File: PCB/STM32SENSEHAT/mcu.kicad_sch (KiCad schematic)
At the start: 5 parts, among them J2 Conn_01x33_Female, J3 Conn_01x33_Female, J4 Conn_01x33_Female, J5 Conn_01x33_Female, J6 Conn_01x10_Pin

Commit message: rework of top level sheet, MCU, power and sensor sheet
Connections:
- net PA10 renamed STM_UART_TX
- net PA9 renamed STM_UART_RX
- net PF6 renamed STM_I2C_SDA
- net PF7 renamed STM_I2C_SCL
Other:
- note added: "I/O INTERFACE"
- note added: "MCU"
- note removed: "16 units apart = 2.54 x 16"
- note removed: "Disco_Connection"
- company: (none) -> IMPERIUM
- title: (none) -> MCU MODULE
- moved on the sheet: J2, J3, J4, J5, J6

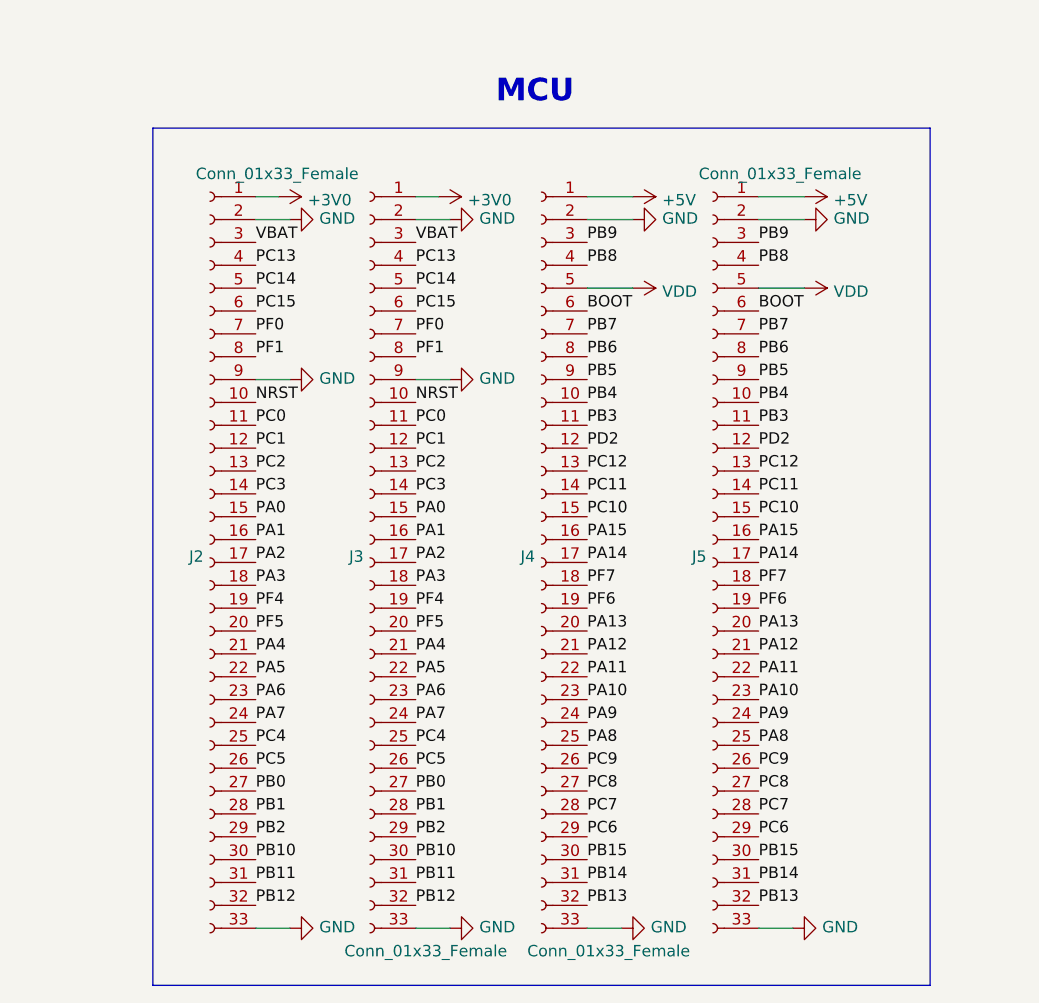
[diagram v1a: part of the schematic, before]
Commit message: Modified the connector symbol for STM32 from 66 pins to 48 pins
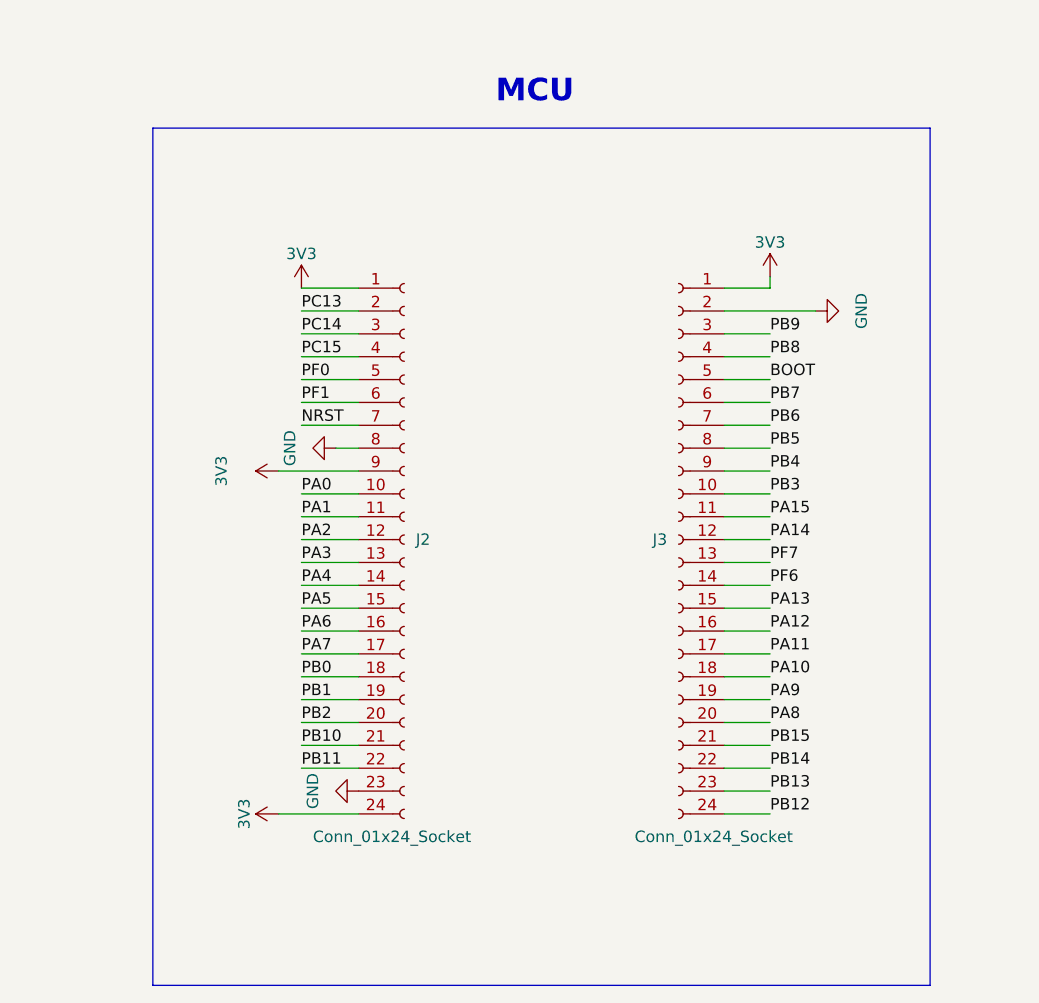
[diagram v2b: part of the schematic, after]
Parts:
- removed J2, J5: Conn_01x33_Female, Connector_PinHeader_2.54mm:PinHeader_1x33_P2.54mm_Vertical, symbol Connector:Conn_01x33_Female
- removed J3, J4: Conn_01x33_Female, Connector_PinSocket_2.54mm:PinSocket_1x33_P2.54mm_Vertical, symbol Connector:Conn_01x33_Female
- added J2, J3: Conn_01x24_Socket, symbol Connector:Conn_01x24_Socket
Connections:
- net BOOT: now also J3.5 (Pin_5)
- net GND: now also J2.23 (Pin_23), J2.8 (Pin_8), J3.2 (Pin_2)
- net NRST: now also J2.7 (Pin_7)
- net PA0: now also J2.10 (Pin_10)
- net PA1: now also J2.11 (Pin_11)
- net PA11: now also J3.17 (Pin_17)
- net PA12: now also J3.16 (Pin_16)
- net PA13: now also J3.15 (Pin_15)
- net PA14: now also J3.12 (Pin_12)
- net PA15: now also J3.11 (Pin_11)
- net PA2: now also J2.12 (Pin_12)
- net PA3: now also J2.13 (Pin_13)
- net PA4: now also J2.14 (Pin_14)
- net PA5: now also J2.15 (Pin_15)
- net PA6: now also J2.16 (Pin_16)
- net PA7: now also J2.17 (Pin_17)
- net PA8: now also J3.20 (Pin_20)
- net PB0: now also J2.18 (Pin_18)
- net PB1: now also J2.19 (Pin_19)
- net PB10: now also J2.21 (Pin_21)
- net PB11: now also J2.22 (Pin_22)
- net PB12: now also J3.24 (Pin_24)
- net PB13: now also J3.23 (Pin_23)
- net PB14: now also J3.22 (Pin_22)
- net PB15: now also J3.21 (Pin_21)
- net PB2: now also J2.20 (Pin_20)
- net PB3: now also J3.10 (Pin_10)
- net PB4: now also J3.9 (Pin_9)
- net PB5: now also J3.8 (Pin_8)
- net PB6: now also J3.7 (Pin_7)
- net PB7: now also J3.6 (Pin_6)
- net PB8: now also J3.4 (Pin_4)
- net PB9: now also J3.3 (Pin_3)
- net PC13: now also J2.2 (Pin_2)
- net PC14: now also J2.3 (Pin_3)
- net PC15: now also J2.4 (Pin_4)
- net PF0: now also J2.5 (Pin_5)
- net PF1: now also J2.6 (Pin_6)
- net STM_I2C_SCL: now also J3.13 (Pin_13)
- net STM_I2C_SDA: now also J3.14 (Pin_14)
- net STM_UART_RX: now also J3.19 (Pin_19)
- net STM_UART_TX: now also J3.18 (Pin_18)
- net VCC: now also J2.1 (Pin_1), J2.24 (Pin_24), J2.9 (Pin_9), J3.1 (Pin_1)
